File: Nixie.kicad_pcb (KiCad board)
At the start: 2 copper layers, 51 parts, among them J1 Led output, J3 Conn_01x03, Q1 Q_NMOS_GSD, U1 74LVC1G79, U2 HV5122, U3 HV5122

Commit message: Update PCB layout, schematic, and documentation exports
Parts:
- added J2: Led Input, Connector_PinHeader_1.00mm:PinHeader_1x20_P1.00mm_Vertical, F.Cu at (143.8, 69.3)
- J1: footprint Connector_PinHeader_1.00mm:PinHeader_1x10_P1.00mm_Vertical -> Connector_PinHeader_1.00mm:PinHeader_1x20_P1.00mm_Vertical
- moved C7 190.0 mm to (244.0, 49.1), turned to -90 degrees
- moved C9 188.6 mm to (241.5, 49.1), turned to -90 degrees
- moved Q1 183.2 mm to (239.3, 34.6)
- moved U1 175.6 mm to (233.2, 34.7)
- moved R18 144.7 mm to (55.1, 42.2)
- moved R5 73.9 mm to (113.2, 36.3)
- moved R9 73.5 mm to (205.4, 36.3)
- moved R4 73.2 mm to (91.0, 36.3)
- moved R6 73.1 mm to (136.8, 36.3)
- moved R7 71.4 mm to (159.7, 36.3)
- moved R8 70.1 mm to (182.6, 36.3)
- moved R26 65.5 mm to (233.9, 40.2), turned to 180 degrees
- moved R27 57.7 mm to (242.8, 53.9), turned to -90 degrees
- moved D1 44.1 mm to (94.9, 52.8), turned to 180 degrees
- moved D2 44.1 mm to (117.8, 52.8), turned to 180 degrees
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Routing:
- net +5V: track 0.00 -> 372.1 mm, vias 0 -> 1
- net /SRB: track 0.00 -> 227.0 mm, vias 0 -> 1
- net /CLK: track 0.00 -> 223.9 mm, vias 0 -> 3
- net /OE: track 0.00 -> 220.7 mm, vias 0 -> 2
- net Net-(U2-Data_Out): track 0.00 -> 194.7 mm, vias 0 -> 2
- net VPP: track 0.00 -> 181.0 mm, vias 0 -> 2
- net /DP1: track 0.00 -> 126.0 mm, vias 0 -> 3
- net /30: track 0.00 -> 111.9 mm, vias 0 -> 2
- net /29: track 0.00 -> 109.0 mm, vias 0 -> 2
- net /31: track 0.00 -> 107.7 mm, vias 0 -> 1
- net /28: track 0.00 -> 106.7 mm, vias 0 -> 2
- net /32: track 0.00 -> 104.5 mm, vias 0 -> 1
- net /27: track 0.00 -> 103.4 mm, vias 0 -> 2
- net /DP2: track 0.00 -> 102.2 mm, vias 0 -> 3
- net /33: track 0.00 -> 98.7 mm, vias 0 -> 1
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- added copper zone on B.Cu, net GND

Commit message: Update PCB layout, schematic exports, design rules, and manufacturing gerbers
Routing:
- net /33: track 98.7 -> 0.00 mm, vias 1 -> 0
- net /34: track 90.0 -> 0.00 mm, vias 1 -> 0
- net /35: track 83.9 -> 0.00 mm, vias 1 -> 0
- net /40: track 80.7 -> 0.00 mm, vias 1 -> 0
- net /36: track 79.2 -> 0.00 mm, vias 1 -> 0
- net /39: track 78.2 -> 0.00 mm, vias 1 -> 0
- net /45: track 77.7 -> 0.00 mm
- net /37: track 77.0 -> 0.00 mm, vias 1 -> 0
- net /38: track 75.9 -> 0.00 mm, vias 1 -> 0
- net /46: track 73.8 -> 0.00 mm
- net /47: track 69.5 -> 0.00 mm
- net Net-(D7-BK): track 67.4 -> 0.00 mm, vias 2 -> 0
- net Net-(D7-GK): track 67.3 -> 0.00 mm, vias 2 -> 0
- net /48: track 65.5 -> 0.00 mm
- net Net-(D7-RK): track 64.1 -> 0.00 mm, vias 2 -> 0
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
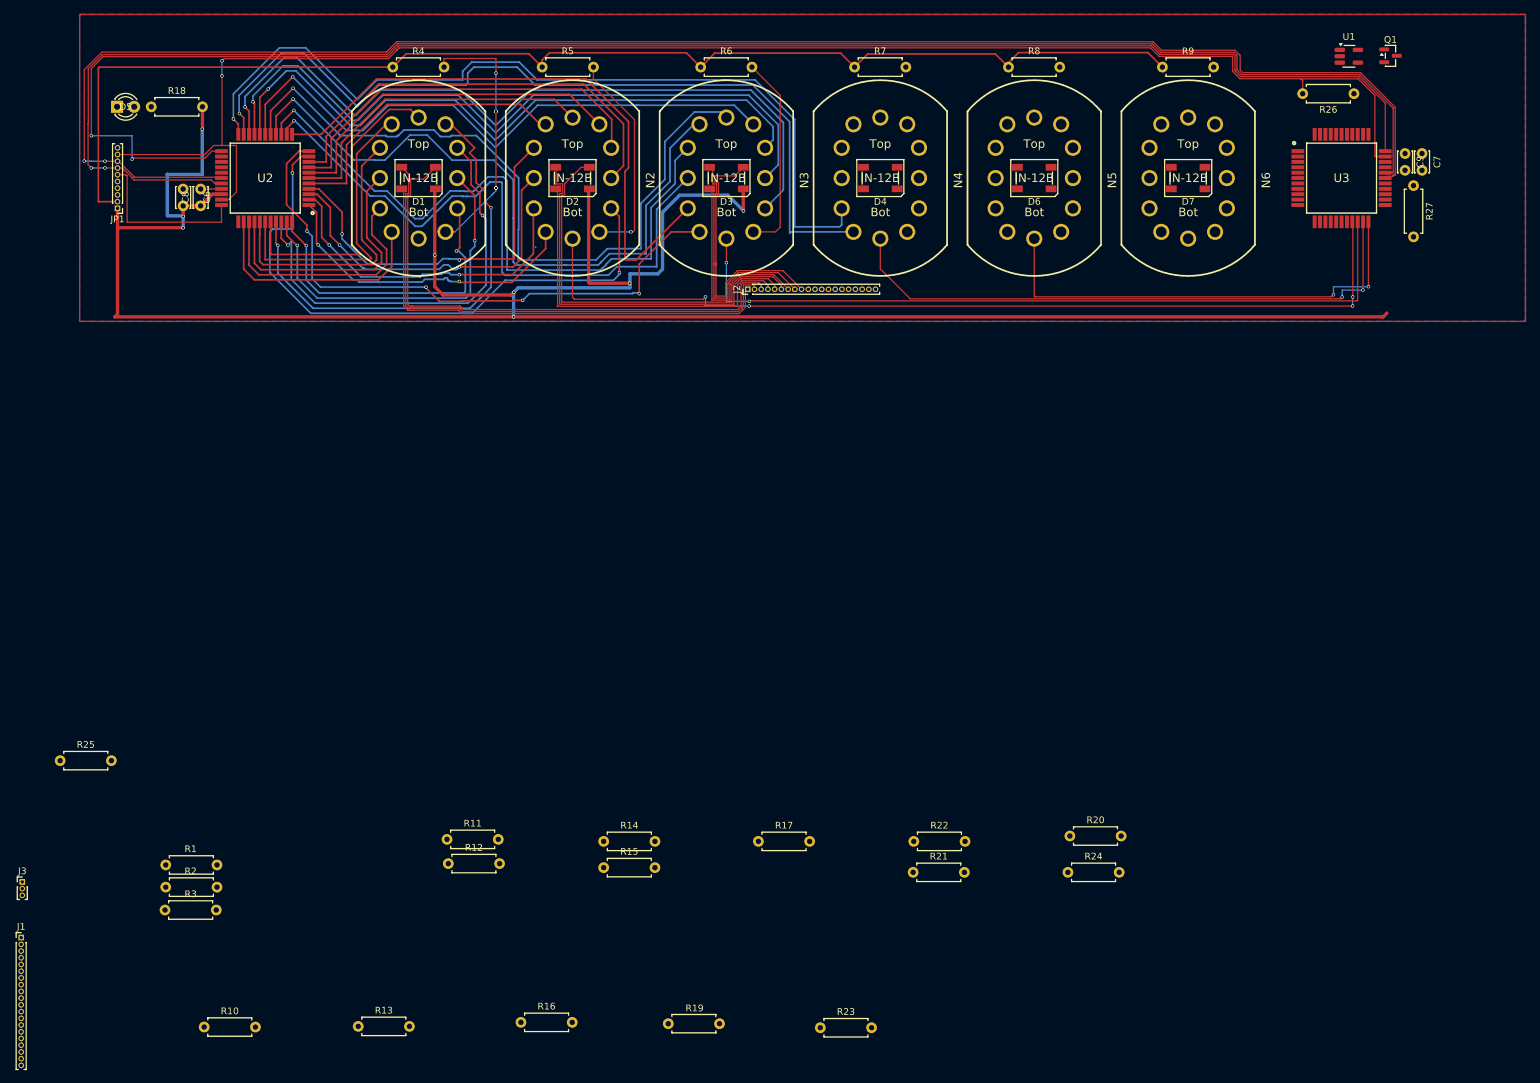
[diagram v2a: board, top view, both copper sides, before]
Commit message: Update PCB layout, design rules, SVG/PDF exports, and gerbers
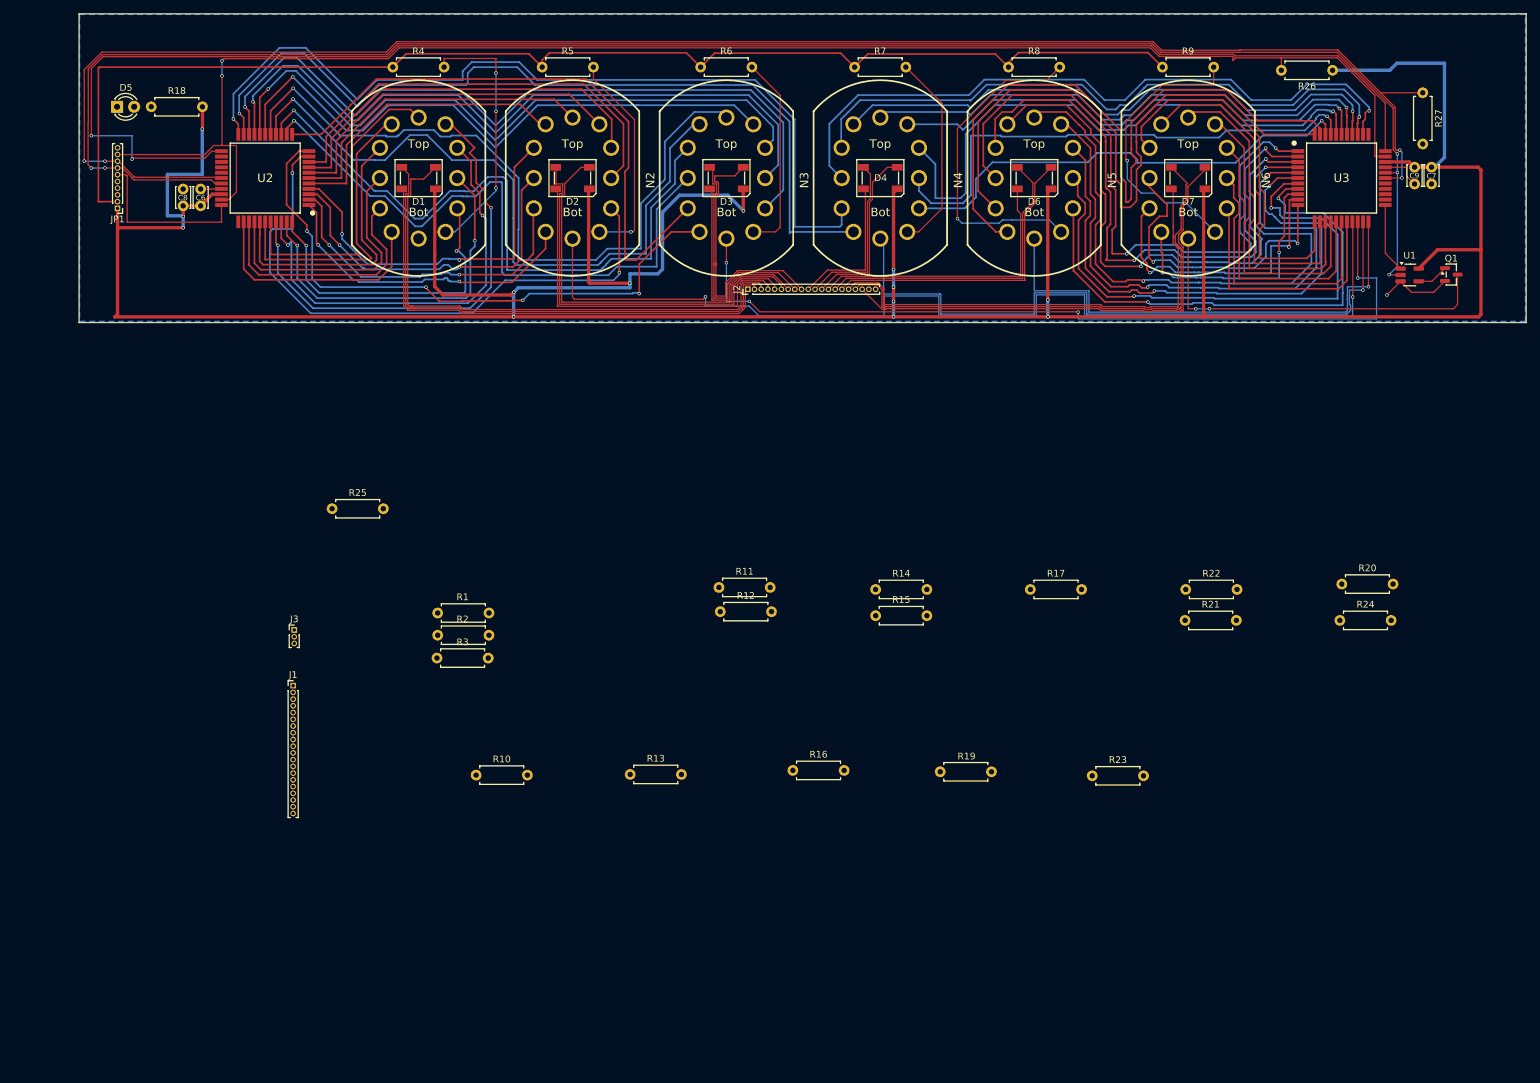
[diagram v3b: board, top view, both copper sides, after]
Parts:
- moved J3 55.1 mm to (76.4, 120.0)
- moved R13 55.1 mm to (126.3, 141.4)
- moved R15 55.1 mm to (162.8, 117.8)
- moved R17 55.1 mm to (185.8, 114.0)
- moved R21 55.1 mm to (208.8, 118.5)
- moved R11 55.1 mm to (139.5, 113.7)
- moved R20 55.1 mm to (232.1, 113.2)
- moved R1 55.1 mm to (97.7, 117.5)
- moved R14 55.1 mm to (162.8, 114.0)
- moved R16 55.1 mm to (150.5, 140.8)
- moved R25 55.1 mm to (82.0, 102.0)
- moved J1 55.1 mm to (76.2, 128.2)
- moved R10 55.1 mm to (103.4, 141.6)
- moved R12 55.1 mm to (139.7, 117.2)
- moved R2 55.1 mm to (97.7, 120.8)
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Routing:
- net +5V: track 350.3 -> 502.0 mm, vias 8 -> 13
- net /41: track 0.00 -> 103.9 mm
- net /33: track 0.00 -> 102.5 mm, vias 0 -> 1
- net /42: track 0.00 -> 95.8 mm
- net /43: track 0.00 -> 95.7 mm, vias 0 -> 2
- net /34: track 0.00 -> 94.3 mm, vias 0 -> 1
- net /46: track 0.00 -> 92.6 mm, vias 0 -> 2
- net /44: track 0.00 -> 89.9 mm, vias 0 -> 2
- net /38: track 0.00 -> 87.8 mm, vias 0 -> 1
- net /47: track 0.00 -> 87.6 mm, vias 0 -> 2
- net /35: track 0.00 -> 87.0 mm, vias 0 -> 1
- net /48: track 0.00 -> 84.0 mm, vias 0 -> 2
- net /49: track 0.00 -> 83.2 mm, vias 0 -> 2
- net /45: track 0.00 -> 83.1 mm, vias 0 -> 2
- net /36: track 0.00 -> 80.9 mm, vias 0 -> 1
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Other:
- board outline added: 215.1 x 45.9 mm

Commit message: Update PCB layout, SVG/PDF exports, and gerber manufacturing files
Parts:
- moved J3 81.1 mm to (147.8, 81.4), turned to -90 degrees
- moved R20 80.5 mm to (156.4, 85.7)
- moved R24 77.3 mm to (156.4, 101.5)
- moved R25 74.5 mm to (156.4, 105.0)
- moved J1 64.5 mm to (138.4, 111.1), turned to 90 degrees
- moved R10 61.9 mm to (130.1, 85.7)
- moved R21 60.0 mm to (156.4, 89.3)
- moved R13 58.3 mm to (143.6, 85.7)
- moved R23 58.3 mm to (156.4, 97.9)
- moved R22 56.6 mm to (156.4, 92.8)
- moved R19 46.1 mm to (143.6, 105.0)
- moved R17 44.0 mm to (143.6, 101.5)
- moved R16 43.5 mm to (143.6, 97.9)
- moved R1 37.8 mm to (130.1, 97.9)
- moved R3 37.7 mm to (130.1, 105.0)
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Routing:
- net /G: track 0.00 -> 91.4 mm
- net /R: track 0.00 -> 87.6 mm
- net /B: track 0.00 -> 83.7 mm
- net Net-(J1-Pin_6): track 0.00 -> 49.4 mm
- net Net-(J1-Pin_5): track 0.00 -> 45.1 mm
- net Net-(J1-Pin_4): track 0.00 -> 37.1 mm
- net Net-(J1-Pin_12): track 0.00 -> 30.8 mm
- net Net-(J1-Pin_13): track 0.00 -> 27.9 mm
- net Net-(J1-Pin_7): track 0.00 -> 27.8 mm
- net Net-(J1-Pin_11): track 0.00 -> 24.8 mm
- net Net-(J1-Pin_8): track 0.00 -> 24.4 mm
- net Net-(J1-Pin_14): track 0.00 -> 23.9 mm
- net Net-(J1-Pin_1): track 0.00 -> 22.7 mm
- net Net-(J1-Pin_9): track 0.00 -> 21.0 mm
- net Net-(J1-Pin_15): track 0.00 -> 20.0 mm
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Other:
- board size 215.1 x 45.9 mm -> 215.1 x 85.8 mm

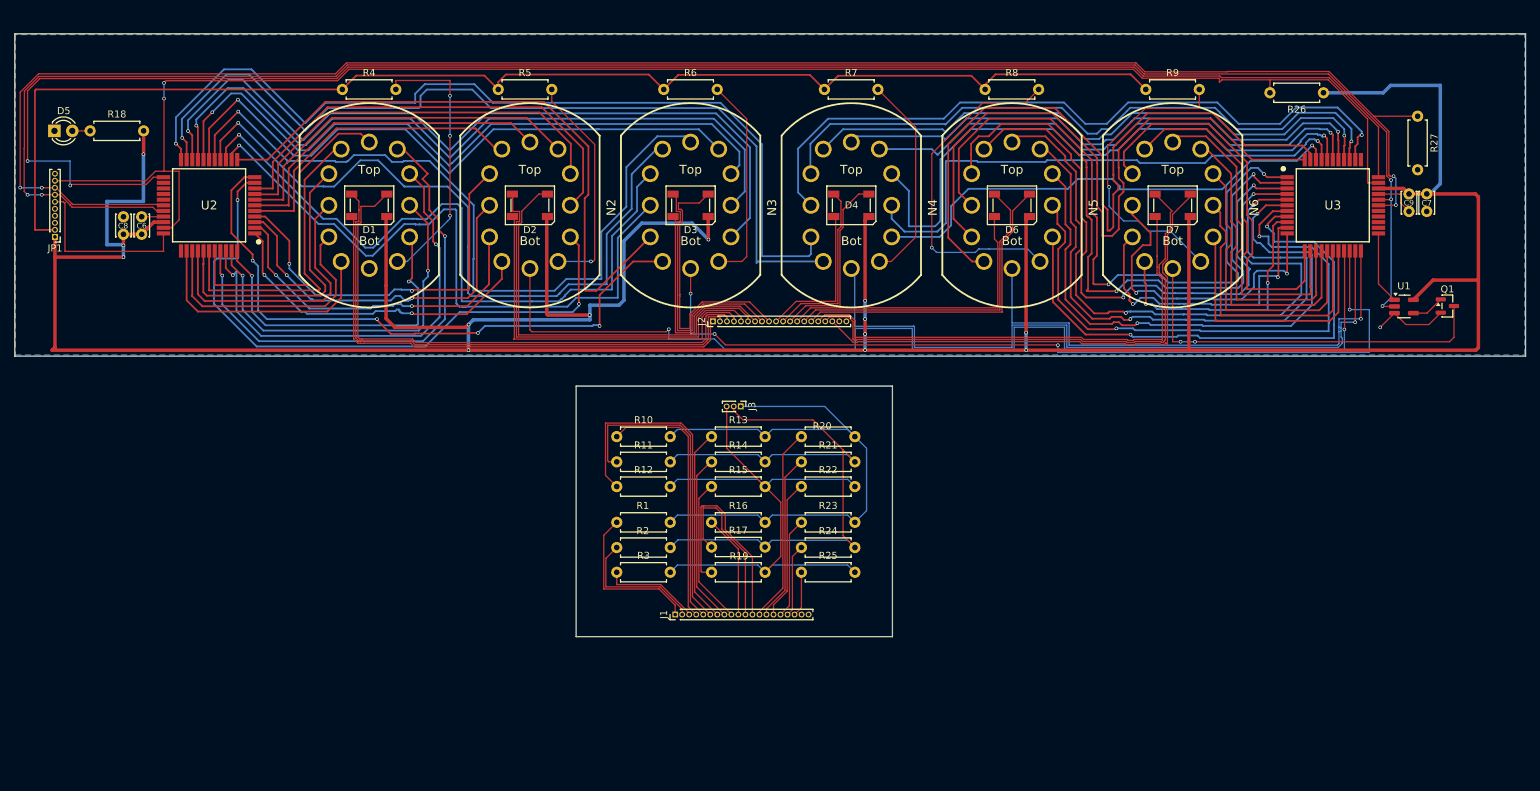
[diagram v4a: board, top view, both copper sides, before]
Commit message: Update schematic connector JP1, PCB routing, BOM, and export files
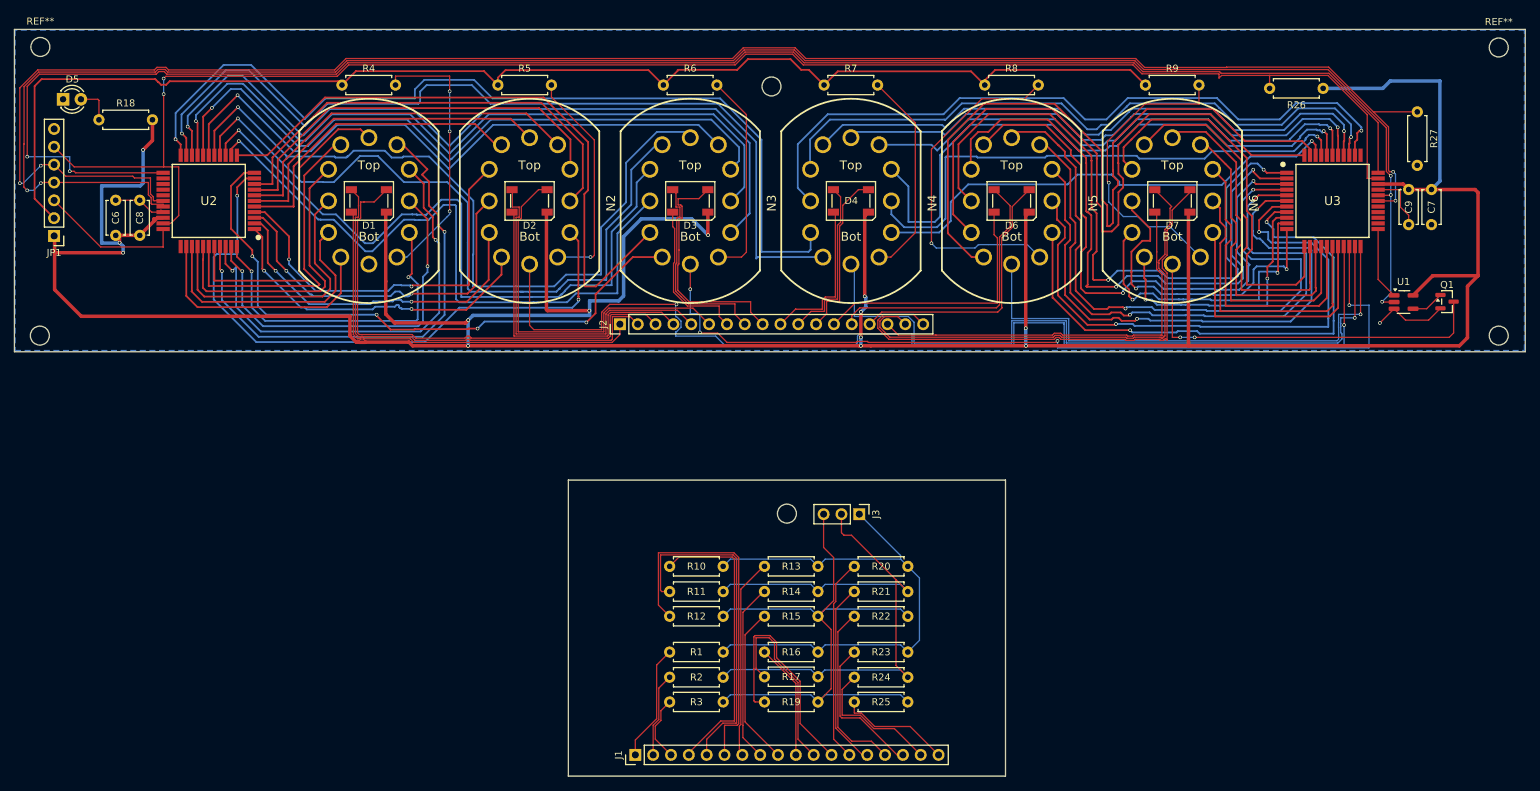
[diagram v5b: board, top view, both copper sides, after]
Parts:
- added REF**: MountingHole_2.7mm, MountingHole:MountingHole_2.7mm, F.Cu at (154.3, 96.7)
- added REF**: MountingHole_2.7mm, MountingHole:MountingHole_2.7mm, F.Cu at (48.0, 71.3)
- added REF**: MountingHole_2.7mm, MountingHole:MountingHole_2.7mm, F.Cu at (255.7, 71.3)
- added REF**: MountingHole_2.7mm, MountingHole:MountingHole_2.7mm, F.Cu at (255.7, 30.3)
- added REF**: MountingHole_2.7mm, MountingHole:MountingHole_2.7mm, F.Cu at (48.0, 30.2)
- added REF**: MountingHole_2.7mm, MountingHole:MountingHole_2.7mm, F.Cu at (152.2, 35.9)
- C6, C7, C8, C9: footprint Capacitor_THT:C_Disc_D3.0mm_W2.0mm_P2.50mm -> Capacitor_THT:C_Disc_D4.7mm_W2.5mm_P5.00mm
- J1, J2: footprint Connector_PinHeader_1.00mm:PinHeader_1x20_P1.00mm_Vertical -> Connector_PinHeader_2.54mm:PinHeader_1x18_P2.54mm_Vertical
- J3: footprint Connector_PinHeader_1.00mm:PinHeader_1x03_P1.00mm_Vertical -> Connector_PinHeader_2.54mm:PinHeader_1x03_P2.54mm_Vertical
- JP1: footprint Connector_PinHeader_1.00mm:PinHeader_1x10_P1.00mm_Vertical -> Connector_PinHeader_2.54mm:PinHeader_1x07_P2.54mm_Vertical
- moved J3 22.8 mm to (164.7, 96.8)
- moved J1 20.8 mm to (132.8, 131.1)
- moved R1 19.9 mm to (137.7, 116.4)
- moved R10 19.9 mm to (137.7, 104.2)
- moved R11 19.9 mm to (137.7, 107.8)
- moved R12 19.9 mm to (137.7, 111.3)
- moved R13 19.9 mm to (151.2, 104.2)
- moved R14 19.9 mm to (151.2, 107.8)
- moved R15 19.9 mm to (151.2, 111.3)
- moved R16 19.9 mm to (151.2, 116.4)
- moved R17 19.9 mm to (151.2, 119.9)
- moved R19 19.9 mm to (151.2, 123.5)
- moved R2 19.9 mm to (137.7, 120.0)
- moved R3 19.9 mm to (137.7, 123.5)
- moved R20 19.9 mm to (163.9, 104.2)
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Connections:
- JP1 pad 3: unconnected-(JP1-Pin_3-Pad3) -> /DIN
- JP1 pad 4: unconnected-(JP1-Pin_4-Pad4) -> /CLK
- JP1 pad 5: unconnected-(JP1-Pin_5-Pad5) -> /OE
- JP1 pad 6: /DIN -> /SRB
- JP1 pad 7: /CLK -> GND
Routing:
- net Net-(D1-RK): track 72.1 -> 57.9 mm
- net Net-(D7-RK): track 70.6 -> 58.2 mm
- net Net-(D1-GK): track 77.9 -> 66.0 mm
- net Net-(D1-BK): track 80.5 -> 70.2 mm
- net Net-(J1-Pin_18): track 6.42 -> 16.0 mm
- net Net-(D3-RK): track 31.9 -> 22.4 mm
- net Net-(J1-Pin_17): track 10.4 -> 19.7 mm
- net Net-(D2-RK): track 53.2 -> 44.3 mm
- net /R: track 87.6 -> 78.9 mm
- net Net-(D3-GK): track 36.7 -> 28.3 mm
- net Net-(D6-BK): track 46.3 -> 38.3 mm
- net GND: track 20.2 -> 27.5 mm
- net Net-(J1-Pin_2): track 19.2 -> 12.0 mm
- net Net-(D2-GK): track 57.9 -> 50.8 mm
- net Net-(J1-Pin_16): track 14.4 -> 21.2 mm
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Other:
- board size 215.1 x 85.8 mm -> 215.1 x 106.3 mm
